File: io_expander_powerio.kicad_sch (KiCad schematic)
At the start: 12 parts, among them U10 ULN2003A, U9 ULN2003A

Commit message: WIP: display
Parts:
- renumbered U9 to U10, U10 to U11
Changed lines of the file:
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@@
   (symbol (lib_id "Transistor_Array:ULN2003A") (at 139.7 101.6 0) (unit 1)
     (in_bom yes) (on_board yes)
-    (property "Reference" "U10" (id 0) (at 139.7 85.09 0))
+    (property "Reference" "U11" (id 0) (at 139.7 85.09 0))
     (property "Value" "ULN2003A" (id 1) (at 139.7 87.63 0))
     (property "Footprint" "Package_SO:SOIC-16_3.9x9.9mm_P1.27mm" (id 2) (at 140.97 115.57 0)
@@
   (symbol (lib_id "Transistor_Array:ULN2003A") (at 139.7 50.8 0) (unit 1)
     (in_bom yes) (on_board yes)
-    (property "Reference" "U9" (id 0) (at 139.7 34.29 0))
+    (property "Reference" "U10" (id 0) (at 139.7 34.29 0))
     (property "Value" "ULN2003A" (id 1) (at 139.7 36.83 0))
     (property "Footprint" "Package_SO:SOIC-16_3.9x9.9mm_P1.27mm" (id 2) (at 140.97 64.77 0)

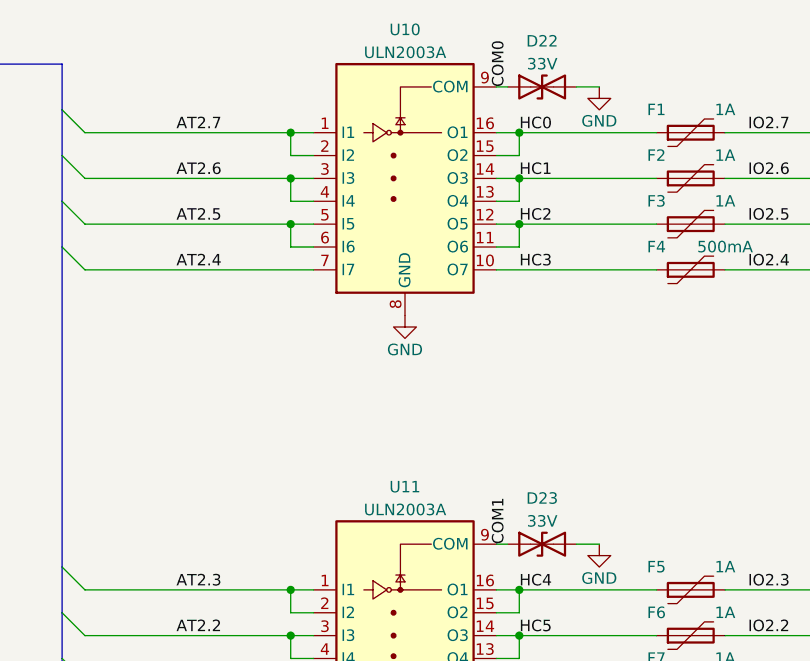
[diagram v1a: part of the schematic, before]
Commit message: rev1.1: Add I2C pullups
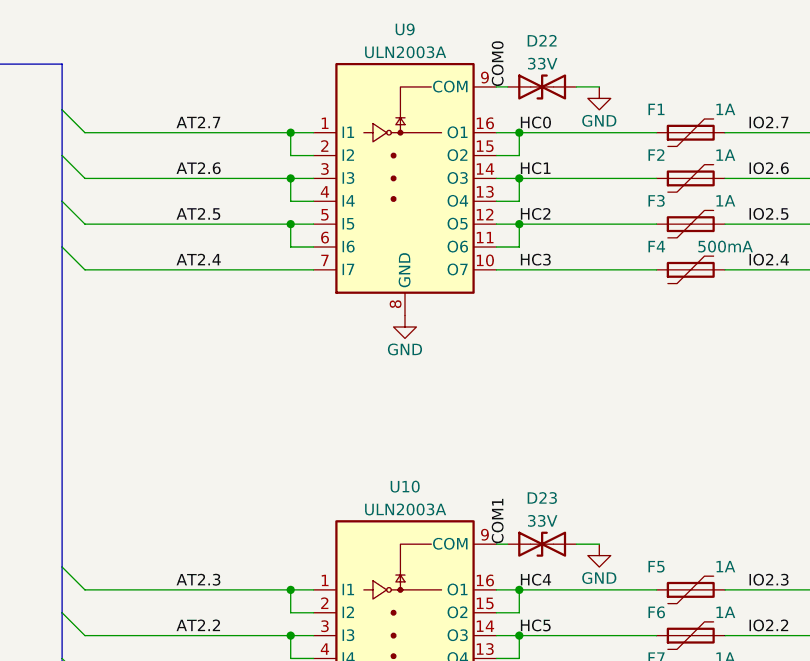
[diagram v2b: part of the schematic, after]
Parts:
- renumbered U11 to U10, U10 to U9
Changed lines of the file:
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@@
   (title_block
     (title "[canbrd] CAN/RS485 IO board")
-    (date "2022-02-24")
-    (rev "1.0")
+    (date "2022-03-18")
+    (rev "1.1")
   )
   (junction (at 152.4 101.6) (diameter 0) (color 0 0 0 0)
@@
   (symbol (lib_id "power:GND") (at 139.7 66.04 0) (unit 1)
     (in_bom yes) (on_board yes)
-    (property "Reference" "#PWR098" (id 0) (at 139.7 72.39 0)
+    (property "Reference" "#PWR0100" (id 0) (at 139.7 72.39 0)
       (effects (font (size 1.27 1.27)) hide)
     )
@@
   (symbol (lib_id "Transistor_Array:ULN2003A") (at 139.7 101.6 0) (unit 1)
     (in_bom yes) (on_board yes)
-    (property "Reference" "U11" (id 0) (at 139.7 85.09 0))
+    (property "Reference" "U10" (id 0) (at 139.7 85.09 0))
     (property "Value" "ULN2003A" (id 1) (at 139.7 87.63 0))
     (property "Footprint" "Package_SO:SOIC-16_3.9x9.9mm_P1.27mm" (id 2) (at 140.97 115.57 0)
@@
   (symbol (lib_id "power:GND") (at 139.7 116.84 0) (unit 1)
     (in_bom yes) (on_board yes)
-    (property "Reference" "#PWR0100" (id 0) (at 139.7 123.19 0)
+    (property "Reference" "#PWR0102" (id 0) (at 139.7 123.19 0)
       (effects (font (size 1.27 1.27)) hide)
     )
@@
   (symbol (lib_id "power:GND") (at 161.29 91.44 0) (unit 1)
     (in_bom yes) (on_board yes)
-    (property "Reference" "#PWR099" (id 0) (at 161.29 97.79 0)
+    (property "Reference" "#PWR0101" (id 0) (at 161.29 97.79 0)
       (effects (font (size 1.27 1.27)) hide)
     )
@@
   (symbol (lib_id "Transistor_Array:ULN2003A") (at 139.7 50.8 0) (unit 1)
     (in_bom yes) (on_board yes)
-    (property "Reference" "U10" (id 0) (at 139.7 34.29 0))
+    (property "Reference" "U9" (id 0) (at 139.7 34.29 0))
     (property "Value" "ULN2003A" (id 1) (at 139.7 36.83 0))
     (property "Footprint" "Package_SO:SOIC-16_3.9x9.9mm_P1.27mm" (id 2) (at 140.97 64.77 0)
@@
   (symbol (lib_id "power:GND") (at 161.29 40.64 0) (unit 1)
     (in_bom yes) (on_board yes)
-    (property "Reference" "#PWR097" (id 0) (at 161.29 46.99 0)
-      (effects (font (size 1.27 1.27)) hide)
-    )
+    (property "Reference" "#PWR099" (id 0) (at 161.29 46.99 0)
+      (effects (font (size 1.27 1.27)) hide)
+    )
